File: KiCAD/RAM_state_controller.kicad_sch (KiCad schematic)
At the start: 2 parts, among them U28 74HC253, U29 74HC253

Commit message: finished schematics and footprint assignments; need to figure out +5v connection issue
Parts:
- U28, U29: footprint (none) -> Package_DIP:DIP-16_W7.62mm
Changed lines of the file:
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@@
 			)
 		)
-		(property "Footprint" ""
+		(property "Footprint" "Package_DIP:DIP-16_W7.62mm"
 			(at 88.9 137.16 0)
 			(effects
@@
 			)
 		)
-		(property "Footprint" ""
+		(property "Footprint" "Package_DIP:DIP-16_W7.62mm"
 			(at 88.9 67.31 0)
 			(effects

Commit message: fix footprint
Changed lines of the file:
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@@
-	)
-	(symbol
-		(lib_id "power:+5V")
-		(at 140.97 17.78 0)
-		(unit 1)
-		(exclude_from_sim no)
-		(in_bom yes)
-		(on_board yes)
-		(dnp no)
-		(fields_autoplaced yes)
-		(property "Reference" "#PWR074"
-			(at 140.97 21.59 0)
-			(effects
-				(font
-					(size 1.27 1.27)
-				)
-				(hide yes)
-			)
-		)
-		(property "Value" "+5V"
-			(at 140.97 12.7 0)
-			(effects
-				(font
-					(size 1.27 1.27)
-				)
-			)
-		)
-		(property "Footprint" ""
-			(at 140.97 17.78 0)
-			(effects
-				(font
-					(size 1.27 1.27)
-				)
-				(hide yes)
-			)
-		)
-		(property "Datasheet" ""
-			(at 140.97 17.78 0)
-			(effects
-				(font
-					(size 1.27 1.27)
-				)
-				(hide yes)
-			)
-		)
-		(property "Description" "Power symbol creates a global label with name \"+5V\""
-			(at 140.97 17.78 0)
-			(effects
-				(font
-					(size 1.27 1.27)
-				)
-				(hide yes)
-			)
-		)
-		(pin "1"
-		)
-		(instances
-			(project "vga_video_card"
-				(path "/53ebbfbe-eaa1-4706-acc1-611a99db7179/a295050b-d209-4efc-8327-c0e97d5127bf/4528f6b5-ae30-4c98-9cf1-00b4b26f8c16"
-					(reference "#PWR074")
-					(unit 1)
-				)
-			)
-		)
 	)
 	(symbol

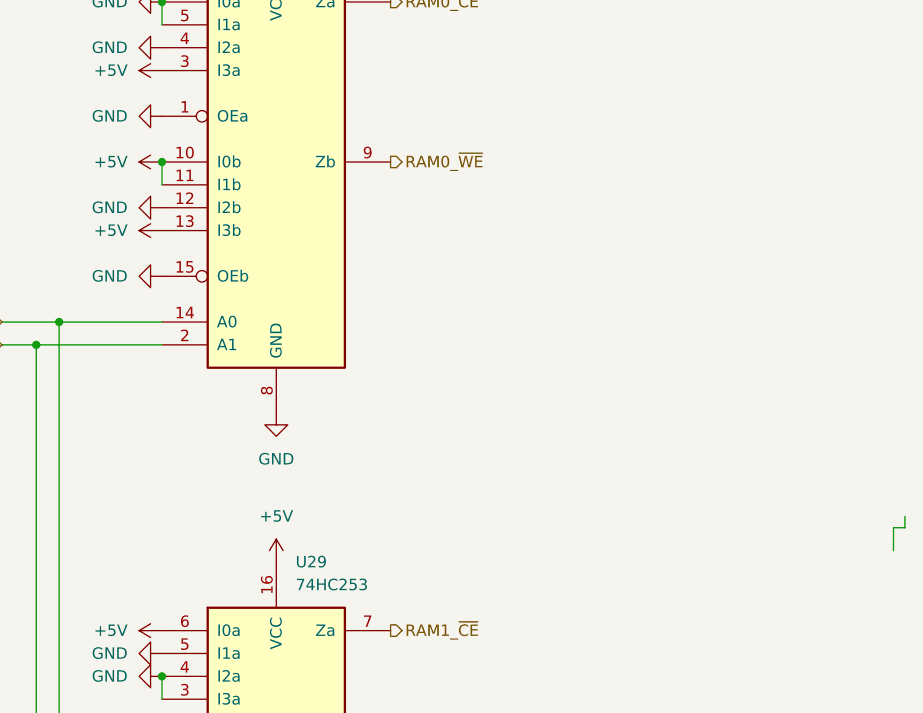
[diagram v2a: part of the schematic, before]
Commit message: fix multiple ERCs that made RAM addrs not connecting
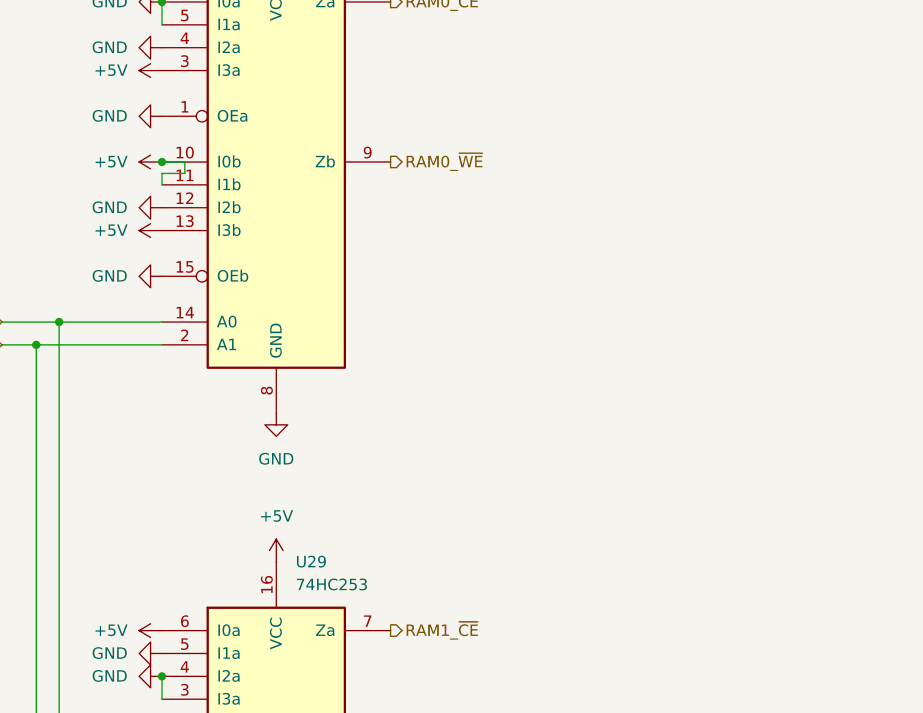
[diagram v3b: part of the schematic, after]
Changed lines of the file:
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@@
+	)
+	(junction
+		(at 76.2 67.31)
+		(diameter 0)
+		(color 0 0 0 0)
 	)
 	(junction
@@
 	)
 	(junction
-		(at 76.2 67.31)
-		(diameter 0)
-		(color 0 0 0 0)
-	)
-	(junction
 		(at 64.77 85.09)
 		(diameter 0)
@@
 		(diameter 0)
 		(color 0 0 0 0)
-	)
-	(wire
-		(pts
-			(xy 76.2 49.53) (xy 76.2 52.07)
-		)
-		(stroke
-			(width 0)
-			(type default)
-		)
 	)
 	(wire
@@
 		(pts
 			(xy 62.23 87.63) (xy 62.23 157.48)
+		)
+		(stroke
+			(width 0)
+			(type default)
+		)
+	)
+	(wire
+		(pts
+			(xy 78.74 68.58) (xy 78.74 67.31)
 		)
 		(stroke
@@
 	(wire
 		(pts
-			(xy 76.2 67.31) (xy 76.2 69.85)
+			(xy 76.2 68.58) (xy 76.2 69.85)
 		)
 		(stroke
@@
 	(wire
 		(pts
-			(xy 157.48 107.95) (xy 157.48 110.49)
+			(xy 76.2 49.53) (xy 76.2 52.07)
 		)
 		(stroke
@@
 	(wire
 		(pts
-			(xy 158.75 107.95) (xy 157.48 107.95)
-		)
-		(stroke
-			(width 0)
-			(type default)
-		)
-	)
-	(wire
-		(pts
-			(xy 158.75 106.68) (xy 158.75 107.95)
+			(xy 76.2 67.31) (xy 78.74 67.31)
 		)
 		(stroke
@@
 		)
 		(stroke
+			(width 0)
+			(type default)
+		)
+	)
+	(wire
+		(pts
+			(xy 76.2 68.58) (xy 78.74 68.58)
+		)
+		(stroke

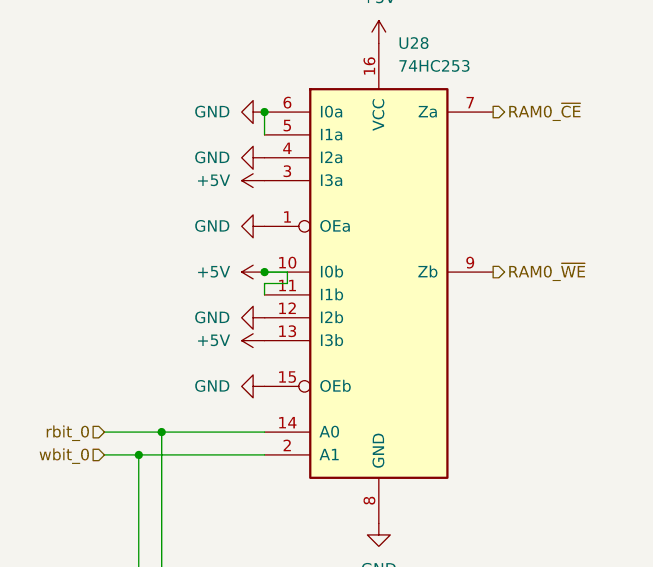
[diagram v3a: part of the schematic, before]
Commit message: resolve ERCs for addr combiner
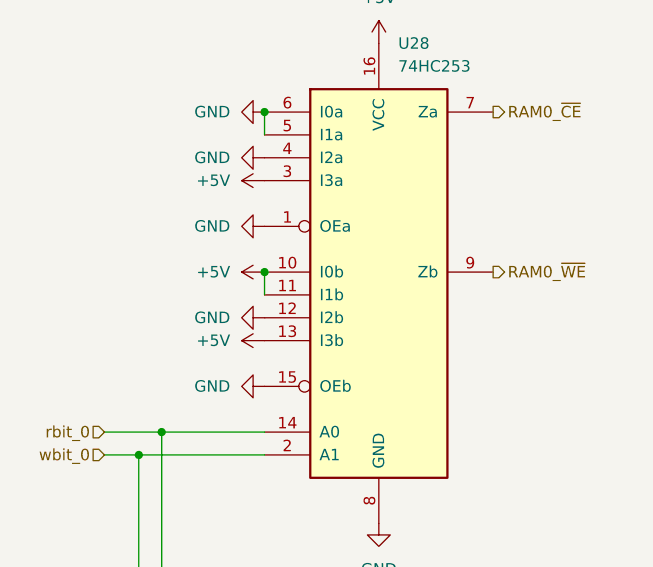
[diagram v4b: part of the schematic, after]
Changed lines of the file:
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@@
 	(paper "A4")
 	(junction
-		(at 62.23 87.63)
+		(at 76.2 67.31)
 		(diameter 0)
 		(color 0 0 0 0)
 	)
 	(junction
-		(at 76.2 67.31)
+		(at 62.23 87.63)
 		(diameter 0)
 		(color 0 0 0 0)
@@
 	(wire
 		(pts
-			(xy 78.74 68.58) (xy 78.74 67.31)
+			(xy 58.42 85.09) (xy 64.77 85.09)
 		)
 		(stroke
@@
 	(wire
 		(pts
-			(xy 58.42 85.09) (xy 64.77 85.09)
+			(xy 76.2 67.31) (xy 76.2 69.85)
 		)
 		(stroke
@@
 	(wire
 		(pts
-			(xy 76.2 68.58) (xy 76.2 69.85)
+			(xy 76.2 142.24) (xy 76.2 144.78)
 		)
 		(stroke
@@
 		(pts
 			(xy 76.2 49.53) (xy 76.2 52.07)
-		)
-		(stroke
-			(width 0)
-			(type default)
-		)
-	)
-	(wire
-		(pts
-			(xy 76.2 142.24) (xy 76.2 144.78)
-		)
-		(stroke
-			(width 0)
-			(type default)
-		)
-	)
-	(wire
-		(pts
-			(xy 76.2 67.31) (xy 78.74 67.31)
 		)
 		(stroke
@@
 		)
 		(stroke
-			(width 0)
-			(type default)
-		)
-	)
-	(wire
-		(pts
-			(xy 76.2 68.58) (xy 78.74 68.58)
-		)
-		(stroke

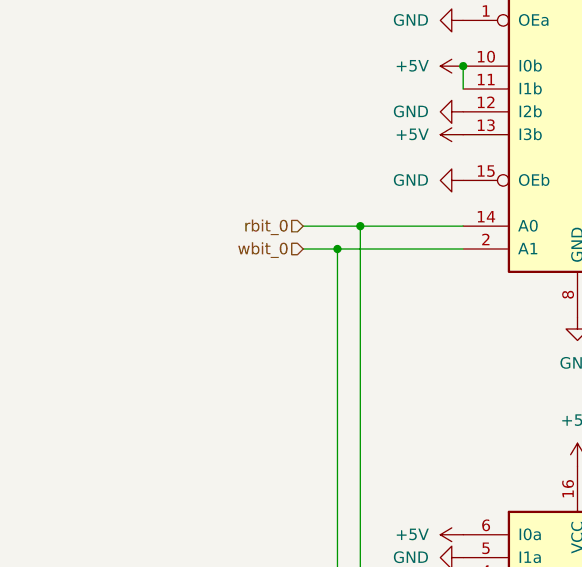
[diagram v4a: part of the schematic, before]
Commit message: add schematics todos for DAC and RAM state controller
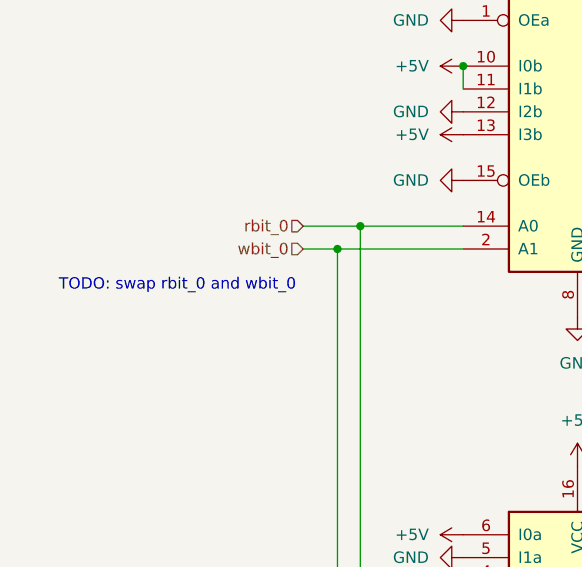
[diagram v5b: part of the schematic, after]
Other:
- note added: "TODO: swap rbit_0 and wbit_0"
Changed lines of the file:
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@@
 	(generator_version "9.0")
 	(paper "A4")
+	(text "TODO: swap rbit_0 and wbit_0"
+		(exclude_from_sim no)
+		(at 44.45 91.694 0)
+		(effects
+			(font
+				(size 1.27 1.27)
+			)
+		)
+	)
 	(junction
 		(at 76.2 67.31)

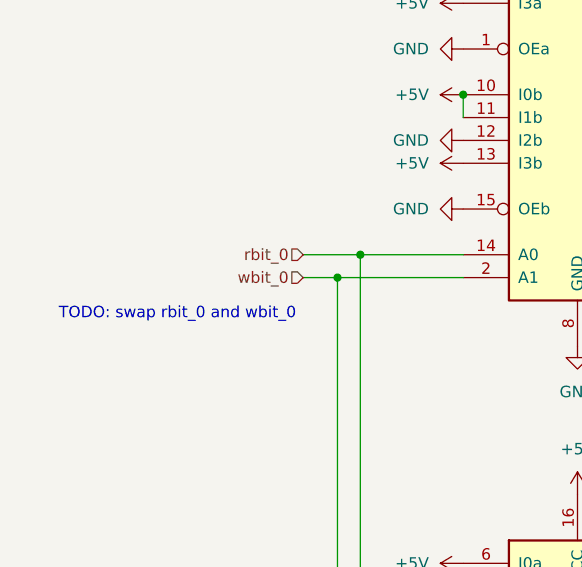
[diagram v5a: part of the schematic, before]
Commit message: update DAC schematics; update pin layout for esp32 connector; update RAM state controller input pin
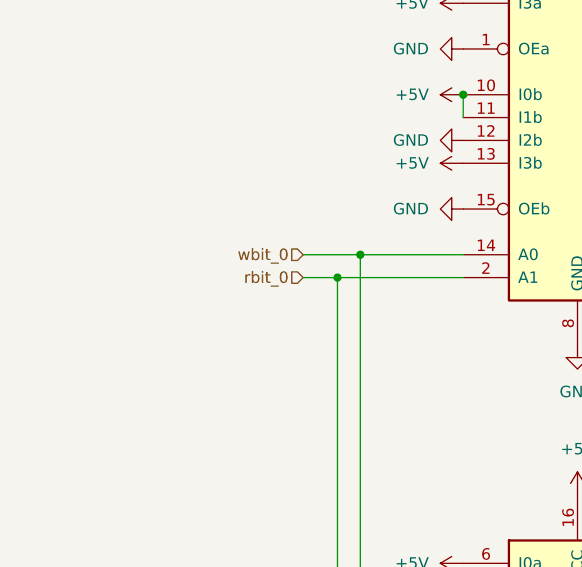
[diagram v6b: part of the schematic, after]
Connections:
- net rbit_0: now also U28.2 (A1), U29.2 (A1); no longer U28.14 (A0), U29.14 (A0)
- net wbit_0: now also U28.14 (A0), U29.14 (A0); no longer U28.2 (A1), U29.2 (A1)
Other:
- note removed: "TODO: swap rbit_0 and wbit_0"
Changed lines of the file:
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@@
 	(generator_version "9.0")
 	(paper "A4")
-	(text "TODO: swap rbit_0 and wbit_0"
-		(exclude_from_sim no)
-		(at 44.45 91.694 0)
-		(effects
-			(font
-				(size 1.27 1.27)
-			)
-		)
-	)
 	(junction
 		(at 76.2 67.31)
@@
 		)
 	)
-	(hierarchical_label "wbit_0"
-		(shape input)
-		(at 58.42 87.63 180)
-		(effects
-			(font
-				(size 1.27 1.27)
-			)
-			(justify right)
-		)
-	)
-	(hierarchical_label "rbit_0"
-		(shape input)
-		(at 58.42 85.09 180)
-		(effects
-			(font
-				(size 1.27 1.27)
-			)
-			(justify right)
-		)
-	)
 	(hierarchical_label "RAM0_~{CE}"
 		(shape output)
@@
 		)
 	)
+	(hierarchical_label "wbit_0"
+		(shape input)
+		(at 58.42 85.09 180)
+		(effects
+			(font
+				(size 1.27 1.27)
+			)
+			(justify right)
+		)
+	)
+	(hierarchical_label "rbit_0"
+		(shape input)
+		(at 58.42 87.63 180)
+		(effects
+			(font
+				(size 1.27 1.27)
+			)
+			(justify right)
+		)
+	)
